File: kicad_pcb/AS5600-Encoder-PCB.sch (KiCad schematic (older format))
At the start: 11 parts, among them IC1 AS5600-ASOM, J1 Conn_01x04_Male, J2 Conn_01x04_Male

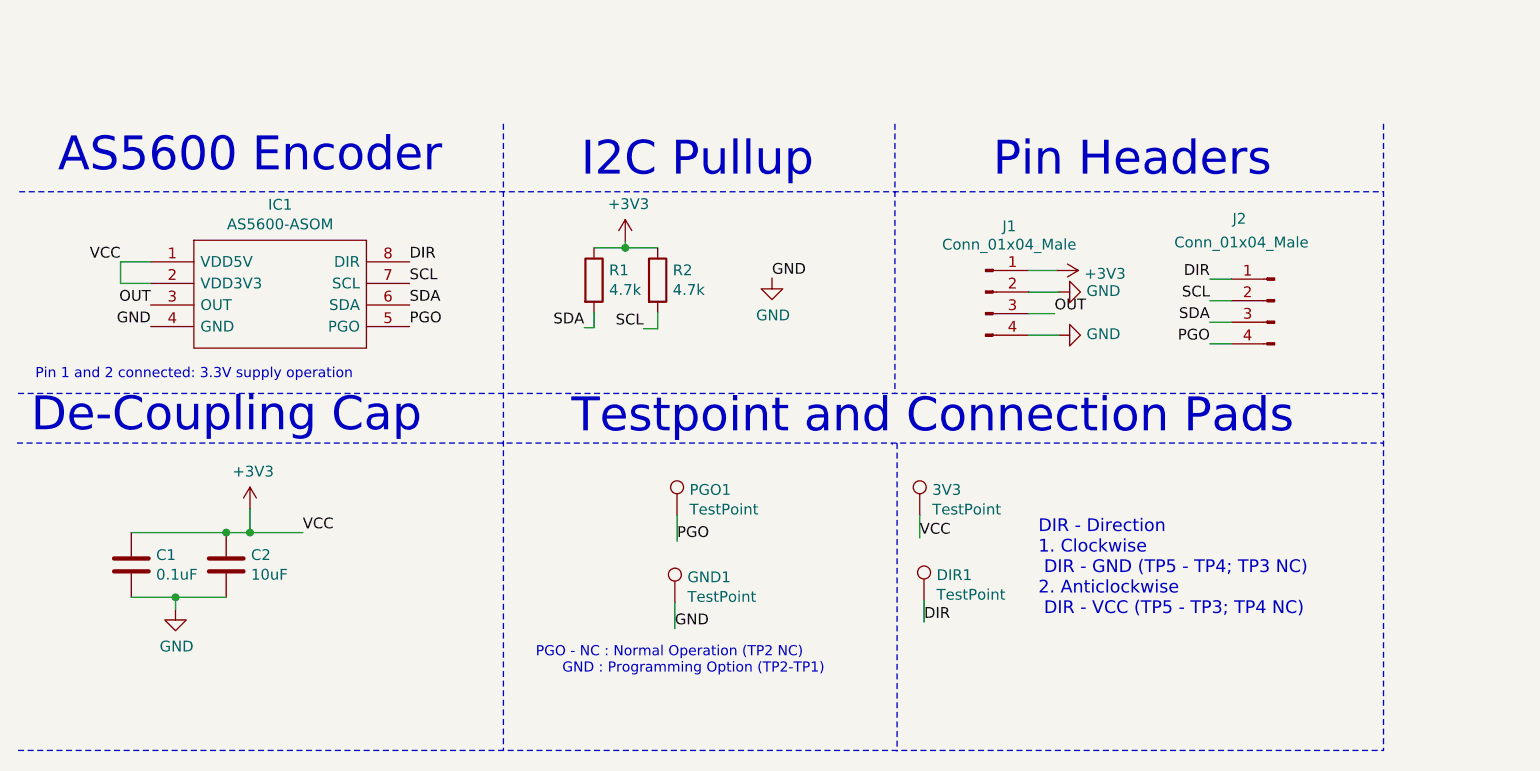
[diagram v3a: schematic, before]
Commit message: Modified and optimized design for 1 layer
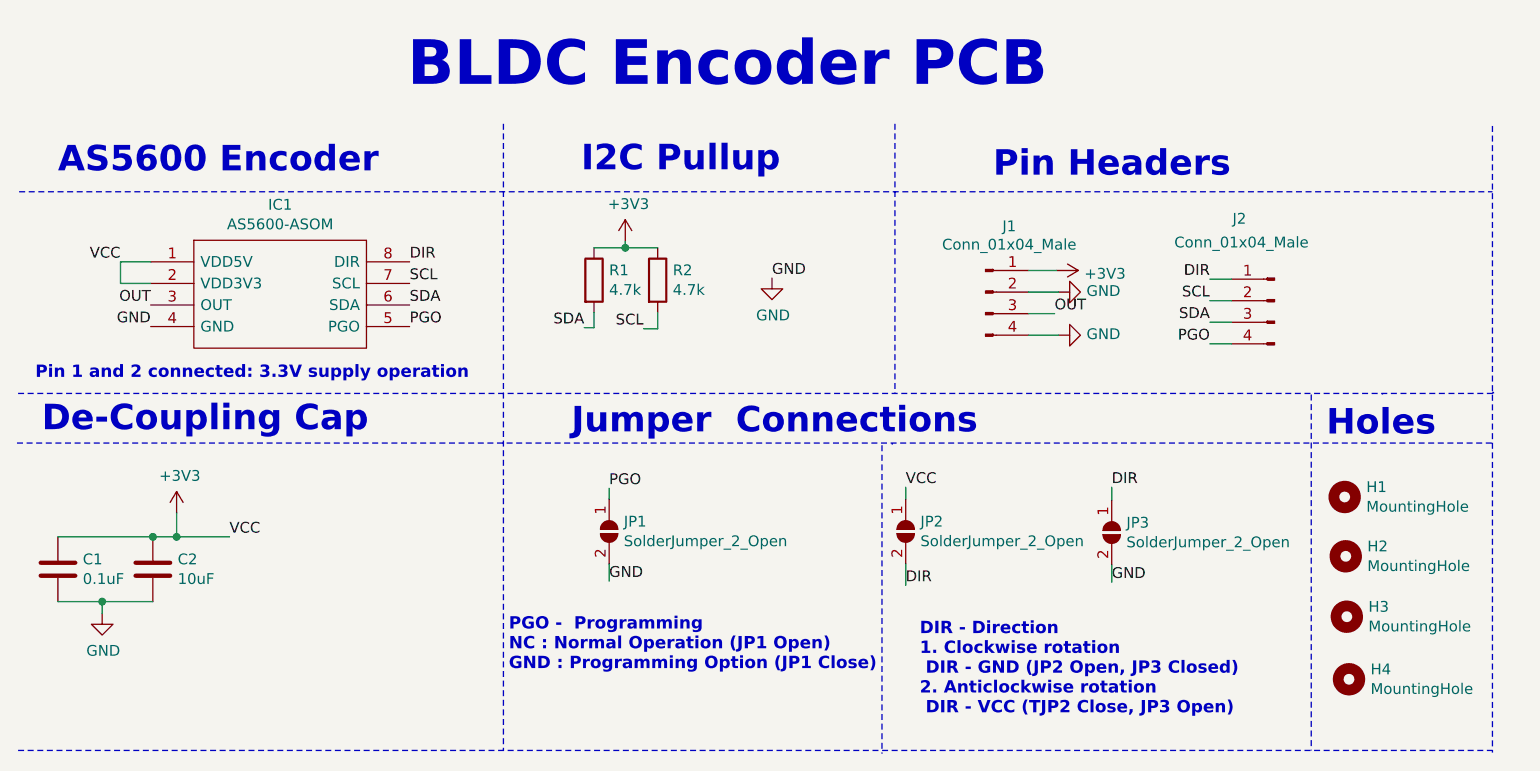
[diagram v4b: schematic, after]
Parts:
- removed 3V3, DIR1, GND1, PGO1: TestPoint, TestPoint:TestPoint_Pad_D2.5mm, symbol Connector:TestPoint
- added H1, H2, H3, H4: MountingHole, MountingHole:MountingHole_2.2mm_M2, symbol Mechanical:MountingHole
- added JP1, JP2, JP3: SolderJumper_2_Open, Jumper:SolderJumper-2_P1.3mm_Open_Pad1.0x1.5mm, symbol Jumper:SolderJumper_2_Open
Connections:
- net +3V3: now also JP2.1 (A)
- net DIR: now also JP2.2 (B), JP3.1 (A)
- net GND: now also JP1.2 (B), JP3.2 (B)
- net PGO: now also JP1.1 (A)
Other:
- note added: "BLDC Encoder PCB"
- note added: "DIR - Direction\n1. Clockwise rotation\n DIR - GND (JP2 Open, JP3 Closed)\n2. Anticlockwise rotation\n DIR - VCC (TJP2 Close, JP3 Open)"
- note added: "Holes"
- note added: "Jumper Connections"
- note added: "PGO - Programming\nNC : Normal Operation (JP1 Open)\nGND : Programming Option (JP1 Close)"
- note removed: "DIR - Direction\n1. Clockwise\n DIR - GND (TP5 - TP4; TP3 NC)\n2. Anticlockwise\n DIR - VCC (TP5 - TP3; TP4 NC)"
- note removed: "PGO - NC : Normal Operation (TP2 NC)\n GND : Programming Option (TP2-TP1)"
- note removed: "Testpoint and Connection Pads"
- moved on the sheet: C1, C2
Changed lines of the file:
@@
 L Device:C C1
 U 1 1 6123A1BF
-P 1000 2520
-F 0 "C1" H 885 2474 50  0000 R CNN
-F 1 "0.1uF" H 885 2565 50  0000 R CNN
-F 2 "Capacitor_SMD:C_1206_3216Metric_Pad1.42x1.75mm_HandSolder" H 1038 2370 50  0001 C CNN
-F 3 "~" H 1000 2520 50  0001 C CNN
-	1    1000 2520
+P 660 2540
+F 0 "C1" H 545 2494 50  0000 R CNN
+F 1 "0.1uF" H 545 2585 50  0000 R CNN
+F 2 "Capacitor_SMD:C_1206_3216Metric_Pad1.42x1.75mm_HandSolder" H 698 2390 50  0001 C CNN
+F 3 "~" H 660 2540 50  0001 C CNN
+	1    660  2540
 	-1   0    0    1
 $EndComp
@@
 L Device:C C2
 U 1 1 6123B253
-P 1440 2520
-F 0 "C2" H 1555 2566 50  0000 L CNN
-F 1 "10uF" H 1555 2475 50  0000 L CNN
-F 2 "Capacitor_SMD:C_1206_3216Metric_Pad1.42x1.75mm_HandSolder" H 1478 2370 50  0001 C CNN
-F 3 "~" H 1440 2520 50  0001 C CNN
-	1    1440 2520
+P 1100 2540
+F 0 "C2" H 1215 2586 50  0000 L CNN
+F 1 "10uF" H 1215 2495 50  0000 L CNN
+F 2 "Capacitor_SMD:C_1206_3216Metric_Pad1.42x1.75mm_HandSolder" H 1138 2390 50  0001 C CNN
+F 3 "~" H 1100 2540 50  0001 C CNN
+	1    1100 2540
 	1    0    0    -1
 $EndComp
@@
 L power:+3V3 #PWR02
 U 1 1 6123DA47
-P 1550 2260
-F 0 "#PWR02" H 1550 2110 50  0001 C CNN
-F 1 "+3V3" H 1565 2433 50  0000 C CNN
-F 2 "" H 1550 2260 50  0001 C CNN
-F 3 "" H 1550 2260 50  0001 C CNN
-	1    1550 2260
+P 1210 2280
+F 0 "#PWR02" H 1210 2130 50  0001 C CNN
+F 1 "+3V3" H 1225 2453 50  0000 C CNN
+F 2 "" H 1210 2280 50  0001 C CNN
+F 3 "" H 1210 2280 50  0001 C CNN
+	1    1210 2280
 	1    0    0    -1
 $EndComp
@@
 	950  1115 950  1215
 Wire Wire Line
-	1795 2370 1550 2370
-Wire Wire Line
-	1000 2370 1440 2370
-Wire Wire Line
-	1440 2370 1550 2370
-Connection ~ 1440 2370
-Connection ~ 1550 2370
-Wire Wire Line
-	1550 2370 1550 2260
-Wire Wire Line
-	1000 2670 1205 2670
+	1455 2390 1210 2390
+Wire Wire Line
+	660  2390 1100 2390
+Wire Wire Line
+	1100 2390 1210 2390
+Connection ~ 1100 2390
+Connection ~ 1210 2390
+Wire Wire Line
+	1210 2390 1210 2280
+Wire Wire Line
+	660  2690 865  2690
 $Comp
 L power:GND #PWR01
 U 1 1 61245C69
-P 1205 2725
-F 0 "#PWR01" H 1205 2475 50  0001 C CNN
-F 1 "GND" H 1210 2552 50  0000 C CNN
-F 2 "" H 1205 2725 50  0001 C CNN
-F 3 "" H 1205 2725 50  0001 C CNN
-	1    1205 2725
-	1    0    0    -1
-$EndComp
-Wire Wire Line
-	1205 2725 1205 2670
-Connection ~ 1205 2670
-Wire Wire Line
-	1205 2670 1440 2670
+P 865 2745
+F 0 "#PWR01" H 865 2495 50  0001 C CNN
+F 1 "GND" H 870 2572 50  0000 C CNN
+F 2 "" H 865 2745 50  0001 C CNN
+F 3 "" H 865 2745 50  0001 C CNN
+	1    865  2745
+	1    0    0    -1
+$EndComp
+Wire Wire Line
+	865  2745 865  2690
+Connection ~ 865  2690
+Wire Wire Line
+	865  2690 1100 2690
 $Comp
 L power:+3V3 #PWR05
@@
 Wire Wire Line
 	5160 1355 5280 1355
-$Comp
-L Connector:TestPoint PGO1
-U 1 1 61273AD3
-P 3530 2290
-F 0 "PGO1" H 3588 2408 50  0000 L CNN
-F 1 "TestPoint" H 3588 2317 50  0000 L CNN
-F 2 "TestPoint:TestPoint_Pad_D2.5mm" H 3730 2290 50  0001 C CNN
-F 3 "~" H 3730 2290 50  0001 C CNN
-	1    3530 2290
-	1    0    0    -1
-$EndComp
-$Comp
-L Connector:TestPoint 3V3
-U 1 1 61274B3F
-P 4655 2290
-F 0 "3V3" H 4713 2408 50  0000 L CNN
-F 1 "TestPoint" H 4713 2317 50  0000 L CNN
-F 2 "TestPoint:TestPoint_Pad_D2.5mm" H 4855 2290 50  0001 C CNN
-F 3 "~" H 4855 2290 50  0001 C CNN
-	1    4655 2290
-	1    0    0    -1
-$EndComp
-$Comp
-L Connector:TestPoint DIR1
-U 1 1 61275699
-P 4675 2685
-F 0 "DIR1" H 4733 2803 50  0000 L CNN
-F 1 "TestPoint" H 4733 2712 50  0000 L CNN
-F 2 "TestPoint:TestPoint_Pad_D2.5mm" H 4875 2685 50  0001 C CNN
-F 3 "~" H 4875 2685 50  0001 C CNN
-	1    4675 2685
-	1    0    0    -1
-$EndComp
-Text Label 3530 2410 0    50   ~ 0
+Text Label 3215 2165 0    50   ~ 0
 PGO
-Text Label 4675 2785 0    50   ~ 0
+Text Label 4590 2615 0    50   ~ 0
 DIR
-Text Label 4655 2395 0    50   ~ 0
+Text Label 4590 2160 0    50   ~ 0
 VCC
-Text Label 1795 2370 0    50   ~ 0
+Text Label 1455 2390 0    50   ~ 0
 VCC
 Wire Wire Line
-	4675 2685 4675 2785
-Wire Wire Line
-	4655 2290 4655 2395
-Wire Wire Line
-	3530 2290 3530 2410
+	4590 2515 4590 2615
+Wire Wire Line
+	4590 2215 4590 2160
+Wire Wire Line
+	3215 2215 3215 2165
 Text Label 950  1115 2    50   ~ 0
 VCC
 Wire Notes Line
-	480  790  6805 790
-Wire Notes Line
 	2725 475  2725 3380
 Wire Notes Line
-	475  3380 6805 3380
-Wire Notes Line
-	475  1725 6800 1725
-Wire Notes Line
 	6800 1725 6800 1730
 Wire Notes Line
-	470  1955 6805 1955
-Wire Notes Line
 	4525 1960 4530 1960
 Wire Notes Line
-	6805 475  6805 3380
-Text Notes 3085 735  0    157  ~ 0
+	7310 485  7310 3390
+Text Notes 3085 710  0    118  ~ 24
 I2C Pullup
-Text Notes 4995 735  0    157  ~ 0
+Text Notes 4995 735  0    118  ~ 24
 Pin Headers
 Wire Notes Line
 	4540 475  4540 1725
-Text Notes 535  1920 0    157  ~ 0
+Text Notes 585  1915 0    118  ~ 24
 De-Coupling Cap
-Text Notes 3040 1925 0    157  ~ 0
-Testpoint and Connection Pads
-Text Notes 2875 3030 0    47   ~ 0
-PGO - NC : Normal Operation (TP2 NC)\n      GND : Programming Option (TP2-TP1)
-Wire Notes Line
-	4550 1955 4550 3385
-Text Notes 555  1665 0    47   ~ 0
+Text Notes 3040 1925 0    118  ~ 24
+Jumper  Connections
+Text Notes 2750 3015 0    57   ~ 11
+PGO -  Programming\nNC : Normal Operation (JP1 Open)\nGND : Programming Option (JP1 Close)
+Wire Notes Line
+	4480 1965 4480 3395
+Text Notes 555  1665 0    57   ~ 11
 Pin 1 and 2 connected: 3.3V supply operation
-Text Notes 5205 2760 0    59   ~ 0
-DIR - Direction\n1. Clockwise\n DIR - GND (TP5 - TP4; TP3 NC)\n2. Anticlockwise\n DIR - VCC (TP5 - TP3; TP4 NC)
+Text Notes 4655 3220 0    57   ~ 11
+DIR - Direction\n1. Clockwise rotation\n DIR - GND (JP2 Open, JP3 Closed)\n2. Anticlockwise rotation\n DIR - VCC (TJP2 Close, JP3 Open)
 Wire Wire Line
 	5160 1255 5300 1255
@@
 	5160 1455 5300 1455
 Wire Wire Line
-	3520 2695 3520 2815
-Text Label 3520 2815 0    50   ~ 0
+	3215 2515 3215 2595
+Text Label 3215 2595 0    50   ~ 0
 GND
-$Comp
-L Connector:TestPoint GND1
-U 1 1 612B9A0F
-P 3520 2695
-F 0 "GND1" H 3578 2813 50  0000 L CNN
-F 1 "TestPoint" H 3578 2722 50  0000 L CNN
-F 2 "TestPoint:TestPoint_Pad_D2.5mm" H 3720 2695 50  0001 C CNN
-F 3 "~" H 3720 2695 50  0001 C CNN
-	1    3520 2695
-	1    0    0    -1
-$EndComp
-Text Notes 660  715  0    157  ~ 0
+Text Notes 660  715  0    118  ~ 24
 AS5600 Encoder
+$Comp
+L Jumper:SolderJumper_2_Open JP1
+U 1 1 6127FCA6
+P 3215 2365
+F 0 "JP1" V 3169 2433 50  0000 L CNN
+F 1 "SolderJumper_2_Open" V 3260 2433 50  0000 L CNN
+F 2 "Jumper:SolderJumper-2_P1.3mm_Open_Pad1.0x1.5mm" H 3215 2365 50  0001 C CNN
+F 3 "~" H 3215 2365 50  0001 C CNN
+	1    3215 2365
+	0    1    1    0
+$EndComp
+$Comp
+L Jumper:SolderJumper_2_Open JP2
+U 1 1 61287850
+P 4590 2365
+F 0 "JP2" V 4544 2433 50  0000 L CNN
+F 1 "SolderJumper_2_Open" V 4635 2433 50  0000 L CNN
+F 2 "Jumper:SolderJumper-2_P1.3mm_Open_Pad1.0x1.5mm" H 4590 2365 50  0001 C CNN
+F 3 "~" H 4590 2365 50  0001 C CNN
+	1    4590 2365
+	0    1    1    0
+$EndComp
+Text Label 5545 2160 0    50   ~ 0
+DIR
+Wire Wire Line
+	5545 2220 5545 2160
+$Comp
+L Jumper:SolderJumper_2_Open JP3
+U 1 1 612930F9
+P 5545 2370
+F 0 "JP3" V 5499 2438 50  0000 L CNN
+F 1 "SolderJumper_2_Open" V 5590 2438 50  0000 L CNN
+F 2 "Jumper:SolderJumper-2_P1.3mm_Open_Pad1.0x1.5mm" H 5545 2370 50  0001 C CNN
+F 3 "~" H 5545 2370 50  0001 C CNN
+	1    5545 2370
+	0    1    1    0
+$EndComp
+Wire Wire Line
+	5545 2520 5545 2600
+Text Label 5545 2600 0    50   ~ 0
+GND
+$Comp
+L Mechanical:MountingHole H1
+U 1 1 612AC280
+P 6625 2205
+F 0 "H1" H 6725 2251 50  0000 L CNN
+F 1 "MountingHole" H 6725 2160 50  0000 L CNN
+F 2 "MountingHole:MountingHole_2.2mm_M2" H 6625 2205 50  0001 C CNN
+F 3 "~" H 6625 2205 50  0001 C CNN
+	1    6625 2205
+	1    0    0    -1
+$EndComp
+$Comp
+L Mechanical:MountingHole H2
+U 1 1 612BAA97
+P 6630 2480
+F 0 "H2" H 6730 2526 50  0000 L CNN
+F 1 "MountingHole" H 6730 2435 50  0000 L CNN
+F 2 "MountingHole:MountingHole_2.2mm_M2" H 6630 2480 50  0001 C CNN
+F 3 "~" H 6630 2480 50  0001 C CNN
+	1    6630 2480
+	1    0    0    -1
+$EndComp
+$Comp
+L Mechanical:MountingHole H3
+U 1 1 612BB1C1
+P 6635 2760
+F 0 "H3" H 6735 2806 50  0000 L CNN
+F 1 "MountingHole" H 6735 2715 50  0000 L CNN
+F 2 "MountingHole:MountingHole_2.2mm_M2" H 6635 2760 50  0001 C CNN
+F 3 "~" H 6635 2760 50  0001 C CNN
+	1    6635 2760
+	1    0    0    -1
+$EndComp
+$Comp
+L Mechanical:MountingHole H4
+U 1 1 612BB910
+P 6645 3050
+F 0 "H4" H 6745 3096 50  0000 L CNN
+F 1 "MountingHole" H 6745 3005 50  0000 L CNN
+F 2 "MountingHole:MountingHole_2.2mm_M2" H 6645 3050 50  0001 C CNN
+F 3 "~" H 6645 3050 50  0001 C CNN
+	1    6645 3050
+	1    0    0    -1
+$EndComp
+Wire Notes Line
+	6470 1730 6470 3380
+Wire Notes Line
+	475  3380 7310 3380
+Wire Notes Line
+	470  1955 7310 1955
+Wire Notes Line
+	7315 1725 7315 1720
+Wire Notes Line
+	7315 1720 7310 1720
+Wire Notes Line
+	475  1725 7315 1725
+Wire Notes Line
+	480  790  7310 790
+Text Notes 6540 1935 0    118  ~ 24
+Holes
+Text Notes 2280 325  0    207  ~ 41
+BLDC Encoder PCB
 $EndSCHEMATC
